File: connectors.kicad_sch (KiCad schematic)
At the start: 4 parts, among them J1 Conn_01x04_Pin, J2 Conn_01x04_Pin, J3 Conn_01x09_Pin, J4 Conn_02x03_Odd_Even

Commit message: Completed symbol-footprint associations.
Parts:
- J1, J2: footprint (none) -> Connector_PinHeader_2.54mm:PinHeader_1x04_P2.54mm_Vertical
- J3: footprint (none) -> Connector_PinHeader_2.54mm:PinHeader_1x09_P2.54mm_Vertical
- J4: footprint (none) -> Connector_PinHeader_2.54mm:PinHeader_2x03_P2.54mm_Vertical
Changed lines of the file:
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@@
 			)
 		)
-		(property "Footprint" ""
+		(property "Footprint" "Connector_PinHeader_2.54mm:PinHeader_1x04_P2.54mm_Vertical"
 			(at 137.16 52.07 0)
 			(effects
@@
 			)
 		)
-		(property "Footprint" ""
+		(property "Footprint" "Connector_PinHeader_2.54mm:PinHeader_2x03_P2.54mm_Vertical"
 			(at 138.43 77.47 0)
 			(effects
@@
 			)
 		)
-		(property "Footprint" ""
+		(property "Footprint" "Connector_PinHeader_2.54mm:PinHeader_1x09_P2.54mm_Vertical"
 			(at 87.63 85.09 0)
 			(effects
@@
 			)
 		)
-		(property "Footprint" ""
+		(property "Footprint" "Connector_PinHeader_2.54mm:PinHeader_1x04_P2.54mm_Vertical"
 			(at 87.63 52.07 0)
 			(effects

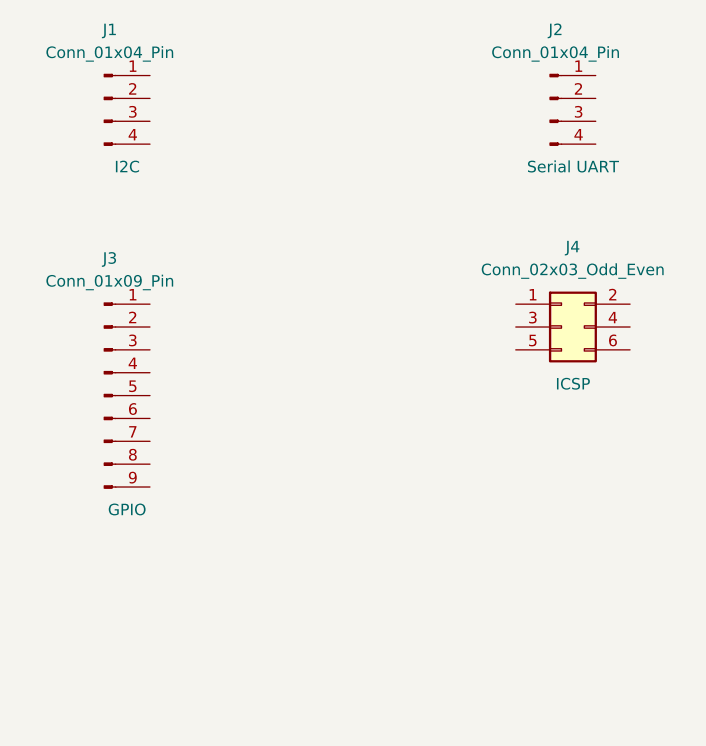
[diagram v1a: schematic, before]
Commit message: Completed wiring in the second sheet.
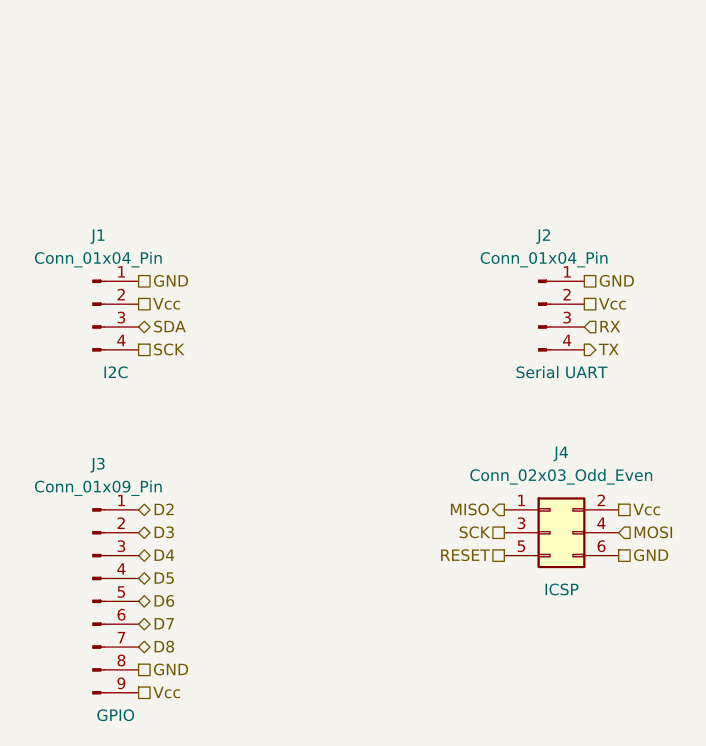
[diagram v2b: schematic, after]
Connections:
- net GND: now reaches J2.1 (Pin_1)
- net GND: now also J1.1 (Pin_1), J3.8 (Pin_8), J4.6 (Pin_6)
- net Vcc: now reaches J2.2 (Pin_2)
- net Vcc: now also J1.2 (Pin_2), J3.9 (Pin_9), J4.2 (Pin_2)
- net RX: now reaches J2.3 (Pin_3)
- net TX: now reaches J2.4 (Pin_4)
- net MISO: now reaches J4.1 (Pin_1)
- net SCK: now reaches J4.3 (Pin_3)
- net SCK: now also J1.4 (Pin_4)
- net MOSI: now reaches J4.4 (Pin_4)
- net RESET: now reaches J4.5 (Pin_5)
- net D2: now reaches J3.1 (Pin_1)
- net D3: now reaches J3.2 (Pin_2)
- net D4: now reaches J3.3 (Pin_3)
- net D5: now reaches J3.4 (Pin_4)
- net D6: now reaches J3.5 (Pin_5)
- net D7: now reaches J3.6 (Pin_6)
- net D8: now reaches J3.7 (Pin_7)
- net SDA: now reaches J1.3 (Pin_3)
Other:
- moved on the sheet: J1, J2, J3, J4

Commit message: Fixed two defects in the schematic.
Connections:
- net SCK: no longer J1.4 (Pin_4)
- new net SCL: J1.4 (Pin_4)
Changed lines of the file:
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@@
 		)
 	)
-	(hierarchical_label "SCK"
+	(hierarchical_label "SCL"
 		(shape passive)
 		(at 91.44 80.01 0)
